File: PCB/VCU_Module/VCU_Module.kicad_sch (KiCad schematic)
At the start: 47 parts, among them J1 5810132011, J10 12V, J12 MCU1, J13 MCU2, J14 5V, J15 3V3, J16 MCU3, J17 MCU4, J2 CN1, J3 CN2, J4 CN3, J5 MCU6, J6 CN4, J7 MCU5, J9 GND, Q1 PJD9P06A-AU_L2_000A1, U3 LMR33640DDDA, U4 LMR33640DDDA

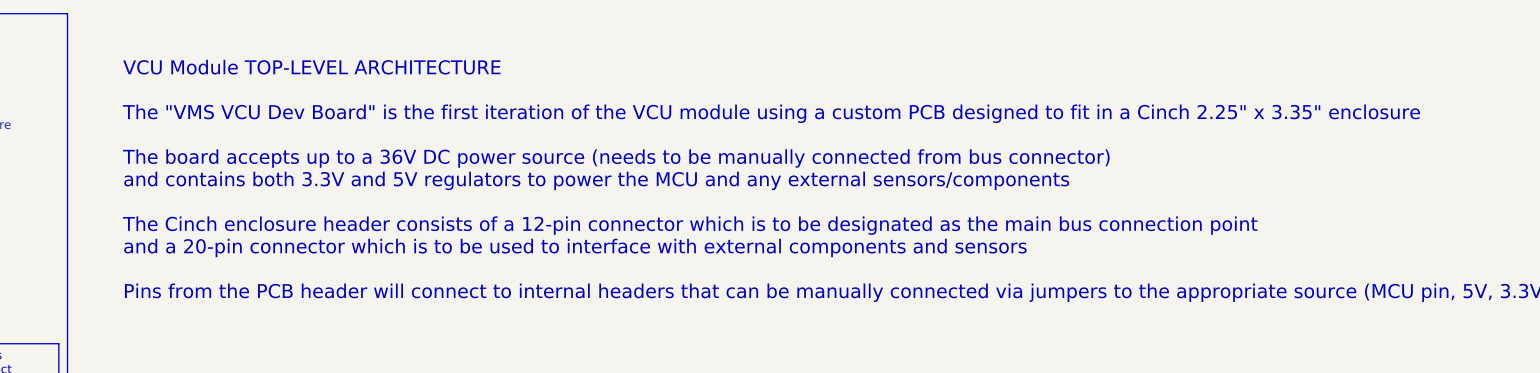
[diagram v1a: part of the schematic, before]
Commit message: Update text in schematic
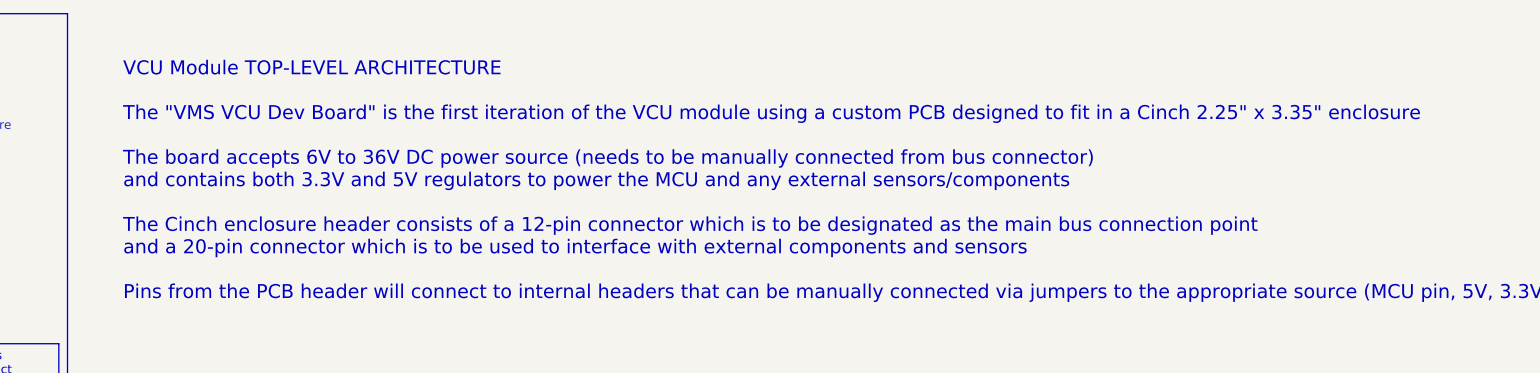
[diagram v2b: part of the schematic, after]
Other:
- note added: "VCU Module TOP-LEVEL ARCHITECTURE The "VMS VCU Dev Board" is the first iteration of the VCU module using a custom PCB designed to fit in a Cinch 2.25" x 3.35" enclosure The board accepts 6V to 36V DC power source (needs to be manually connected from bus connector) and contains both 3.3V and 5V regulators to power the MCU and any external sensors/components The Cinch enclosure header consists of a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"
- note removed: "VCU Module TOP-LEVEL ARCHITECTURE The "VMS VCU Dev Board" is the first iteration of the VCU module using a custom PCB designed to fit in a Cinch 2.25" x 3.35" enclosure The board accepts up to a 36V DC power source (needs to be manually connected from bus connector) and contains both 3.3V and 5V regulators to power the MCU and any external sensors/components The Cinch enclosure header consists of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"
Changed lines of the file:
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@@
 		)
 	)
-	(text "VCU Module TOP-LEVEL ARCHITECTURE\n\nThe \"VMS VCU Dev Board\" is the first iteration of the VCU module using a custom PCB designed to fit in a Cinch 2.25\" x 3.35\" enclosure\n\nThe board accepts up to a 36V DC power source (needs to be manually connected from bus connector) \nand contains both 3.3V and 5V regulators to power the MCU and any external sensors/components\n\nThe Cinch enclosure header consists of a 12-pin connector which is to be designated as the main bus connection point \nand a 20-pin connector which is to be used to interface with external components and sensors\n\nPins from the PCB header will connect to internal headers that can be manually connected via jumpers to the appropriate source (MCU pin, 5V, 3.3V, CAN H/L, GND, etc.) \n\n"
+	(text "VCU Module TOP-LEVEL ARCHITECTURE\n\nThe \"VMS VCU Dev Board\" is the first iteration of the VCU module using a custom PCB designed to fit in a Cinch 2.25\" x 3.35\" enclosure\n\nThe board accepts 6V to 36V DC power source (needs to be manually connected from bus connector) \nand contains both 3.3V and 5V regulators to power the MCU and any external sensors/components\n\nThe Cinch enclosure header consists of a 12-pin connector which is to be designated as the main bus connection point \nand a 20-pin connector which is to be used to interface with external components and sensors\n\nPins from the PCB header will connect to internal headers that can be manually connected via jumpers to the appropriate source (MCU pin, 5V, 3.3V, CAN H/L, GND, etc.) \n\n"
 		(exclude_from_sim no)
 		(at 124.968 38.862 0)
